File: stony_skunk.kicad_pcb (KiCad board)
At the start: 2 copper layers, 50 x 50 mm, 37 parts, among them P1 CURRENT/BUTTONS/DC, P2 LCD, P3 RELAY, P4 NFC, P5 FTDI, P6 RESET, P7 PROG, Q1 Q_NMOS_GSD, Q2 Q_NMOS_GSD, U1 NCP1117ST33T3G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

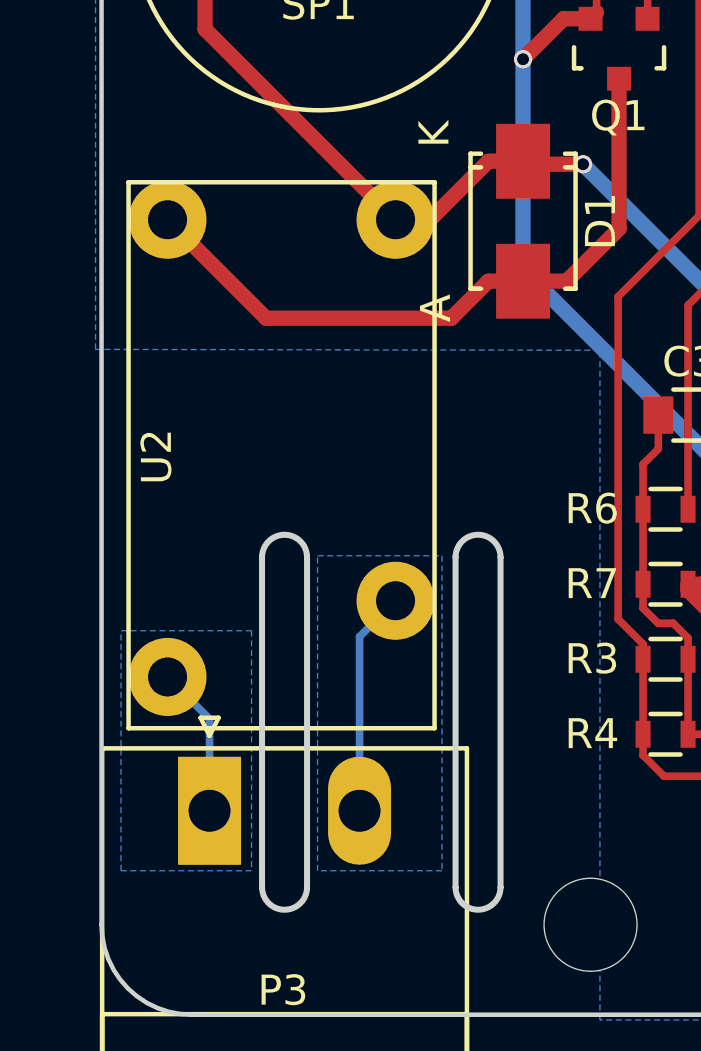
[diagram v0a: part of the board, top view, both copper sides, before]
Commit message: Flip relay to correct orientation
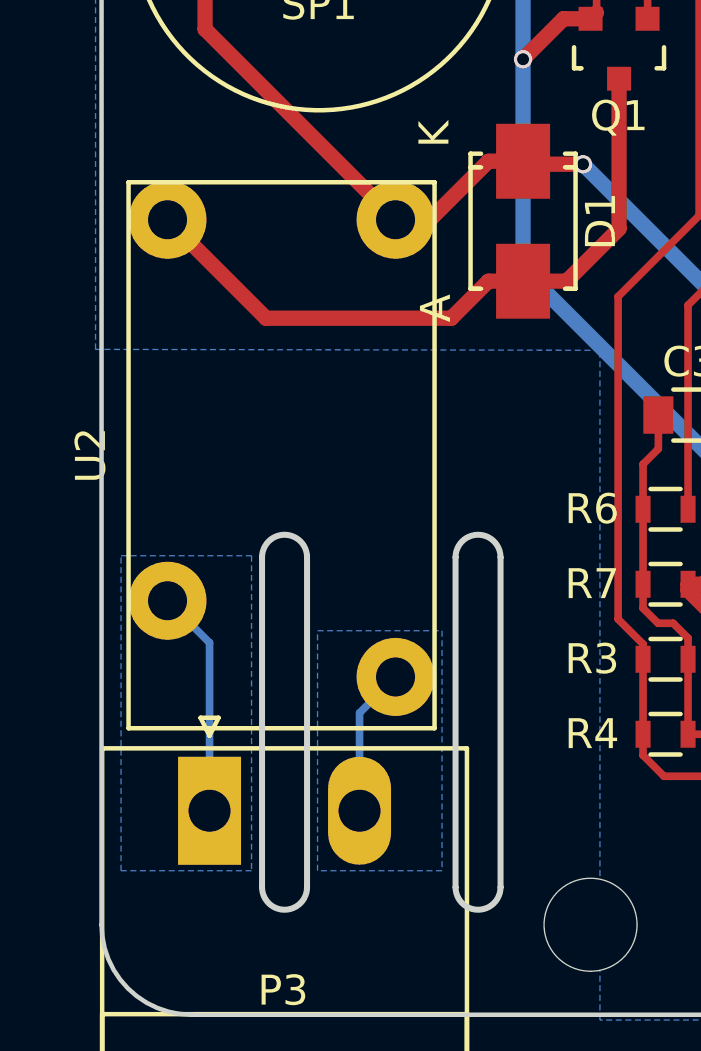
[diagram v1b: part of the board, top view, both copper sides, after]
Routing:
- net Net-(P3-Pad2): track 8.63 -> 4.96 mm
- net Net-(P3-Pad1): track 5.04 -> 7.58 mm
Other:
- board text added: "timhawes.com/ss2 edinburghhacklab.com"
- board text removed: "timhawes.com/ss1 edinburghhacklab.com"
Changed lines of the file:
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@@
-(kicad_pcb (version 4) (host pcbnew 4.0.4-stable)
+(kicad_pcb (version 4) (host pcbnew 4.0.4+dfsg1-stable)
   (general
     (links 76)
     (no_connects 0)
-    (area 60.374999 56.274999 110.525001 106.425001)
+    (area 56.149971 50.269799 114.800829 112.179)
     (thickness 1.6)
     (drawings 22)
-    (tracks 330)
+    (tracks 329)
     (zones 0)
     (modules 37)
@@
   (page A4)
   (layers
-    (0 F.Cu signal hide)
+    (0 F.Cu signal)
     (31 B.Cu signal)
     (32 B.Adhes user)
@@
     )
   )
-  (module timhawes:TE_OJ_RELAY (layer F.Cu)
-    (at 66.45 87.7 270)
-    (fp_text reference U2 (at 0.05 4.15 270) (layer F.SilkS)
-      (effects (font (size 1 1) (thickness 0.15)))
-    )
-    (fp_text value RELAY (at 0 7.75 270) (layer F.Fab)
-      (effects (font (size 1 1) (thickness 0.15)))
-    )
-    (fp_line (start -9.1 -5.1) (end 9.1 -5.1) (layer F.SilkS) (width 0.15))
-    (fp_line (start 9.1 -5.1) (end 9.1 5.1) (layer F.SilkS) (width 0.15))
-    (fp_line (start 9.1 5.1) (end -9.1 5.1) (layer F.SilkS) (width 0.15))
-    (fp_line (start -9.1 -5.1) (end -9.1 5.1) (layer F.SilkS) (width 0.15))
-    (pad 1 thru_hole circle (at -7.85 -3.8 270) (size 2.6 2.6) (drill 1.3) (layers *.Cu *.Mask)
-      (net 1 +5V))
-    (pad 2 thru_hole circle (at -7.85 3.8 270) (size 2.6 2.6) (drill 1.3) (layers *.Cu *.Mask)
-      (net 4 "Net-(D1-Pad2)"))
-    (pad 3 thru_hole circle (at 7.39 3.8 270) (size 2.6 2.6) (drill 1.3) (layers *.Cu *.Mask)
-      (net 8 "Net-(P3-Pad1)"))
-    (pad 4 thru_hole circle (at 4.85 -3.8 270) (size 2.6 2.6) (drill 1.3) (layers *.Cu *.Mask)
-      (net 9 "Net-(P3-Pad2)"))
-  )
   (module timhawes:MountingHole_M3+ (layer F.Cu)
     (at 107.45 95.4)
@@
     (pad "" np_thru_hole circle (at 0 0) (size 3.1 3.1) (drill 3.1) (layers *.Cu))
   )
+  (module timhawes:TE_OJ_RELAY (layer F.Cu)
+    (at 66.45 87.7 270)
+    (fp_text reference U2 (at 0 6.35 450) (layer F.SilkS)
+      (effects (font (size 1 1) (thickness 0.15)))
+    )
+    (fp_text value RELAY (at 0 7.75 270) (layer F.Fab)
+      (effects (font (size 1 1) (thickness 0.15)))
+    )
+    (fp_line (start -9.1 5.1) (end 9.1 5.1) (layer F.SilkS) (width 0.15))
+    (fp_line (start 9.1 5.1) (end 9.1 -5.1) (layer F.SilkS) (width 0.15))
+    (fp_line (start 9.1 -5.1) (end -9.1 -5.1) (layer F.SilkS) (width 0.15))
+    (fp_line (start -9.1 5.1) (end -9.1 -5.1) (layer F.SilkS) (width 0.15))
+    (pad 2 thru_hole circle (at -7.85 3.8 270) (size 2.6 2.6) (drill 1.3) (layers *.Cu *.Mask)
+      (net 4 "Net-(D1-Pad2)"))
+    (pad 1 thru_hole circle (at -7.85 -3.8 270) (size 2.6 2.6) (drill 1.3) (layers *.Cu *.Mask)
+      (net 1 +5V))
+    (pad 4 thru_hole circle (at 7.39 -3.8 270) (size 2.6 2.6) (drill 1.3) (layers *.Cu *.Mask)
+      (net 9 "Net-(P3-Pad2)"))
+    (pad 3 thru_hole circle (at 4.85 3.8 270) (size 2.6 2.6) (drill 1.3) (layers *.Cu *.Mask)
+      (net 8 "Net-(P3-Pad1)"))
+  )
   (gr_text - (at 104.4 98.8) (layer F.SilkS)
     (effects (font (size 1.5 1.5) (thickness 0.3)))
@@
     (effects (font (size 1.5 1.5) (thickness 0.3)))
   )
-  (gr_text "timhawes.com/ss1\nedinburghhacklab.com" (at 85.45 60.7) (layer B.SilkS)
+  (gr_text "timhawes.com/ss2\nedinburghhacklab.com" (at 85.45 60.7) (layer B.SilkS)
     (effects (font (size 1.5 1.5) (thickness 0.3)) (justify mirror))
   )
@@
   (segment (start 92.6846 96.1644) (end 96.3356 96.1644) (width 0.254) (layer F.Cu) (net 7))
   (segment (start 92.6846 93.6244) (end 92.6846 96.1644) (width 0.254) (layer F.Cu) (net 7))
-  (segment (start 64.05 99.55) (end 64.05 96.49) (width 0.254) (layer B.Cu) (net 8))
-  (segment (start 64.05 96.49) (end 62.65 95.09) (width 0.254) (layer B.Cu) (net 8))
-  (segment (start 69.05 99.55) (end 69.05 93.75) (width 0.254) (layer B.Cu) (net 9))
-  (segment (start 69.05 93.75) (end 70.25 92.55) (width 0.254) (layer B.Cu) (net 9))
-  (segment (start 68.75 98.7) (end 69.55 99.5) (width 0.25) (layer B.Cu) (net 9))
+  (segment (start 64.05 99.55) (end 64.05 93.95) (width 0.254) (layer B.Cu) (net 8))
+  (segment (start 64.05 93.95) (end 62.65 92.55) (width 0.254) (layer B.Cu) (net 8))
+  (segment (start 69.05 99.55) (end 69.05 96.29) (width 0.254) (layer B.Cu) (net 9))
+  (segment (start 69.05 96.29) (end 70.25 95.09) (width 0.254) (layer B.Cu) (net 9))
   (segment (start 103 68.3) (end 102.3 69) (width 0.254) (layer F.Cu) (net 10))
   (segment (start 102.3 69) (end 102.1 69) (width 0.254) (layer F.Cu) (net 10))
@@
     (polygon
       (pts
-        (xy 67.65 91.05) (xy 71.8 91.05) (xy 71.8 101.55) (xy 67.65 101.55)
+        (xy 67.65 93.55) (xy 71.8 93.55) (xy 71.8 101.55) (xy 67.65 101.55)
       )
     )
@@
     (min_thickness 0.254)
     (keepout (tracks not_allowed) (vias not_allowed) (copperpour not_allowed))
-    (fill yes (arc_segments 16) (thermal_gap 0.508) (thermal_bridge_width 0.508))
+    (fill (arc_segments 16) (thermal_gap 0.508) (thermal_bridge_width 0.508))
     (polygon
       (pts
@@
     (polygon
       (pts
-        (xy 65.45 93.55) (xy 65.45 101.55) (xy 61.1 101.55) (xy 61.1 93.55)
+        (xy 65.45 91.05) (xy 65.45 101.55) (xy 61.1 101.55) (xy 61.1 91.05)
       )
     )
@@
     (polygon
       (pts
-        (xy 67.65 91.05) (xy 71.8 91.05) (xy 71.8 101.55) (xy 67.65 101.55)
+        (xy 67.65 93.55) (xy 71.8 93.55) (xy 71.8 101.55) (xy 67.65 101.55)
       )
     )
@@
     (polygon
       (pts
-        (xy 61.1 93.55) (xy 65.45 93.55) (xy 65.45 101.55) (xy 61.1 101.55)
+        (xy 61.1 91.05) (xy 65.45 91.05) (xy 65.45 101.55) (xy 61.1 101.55)
       )
     )

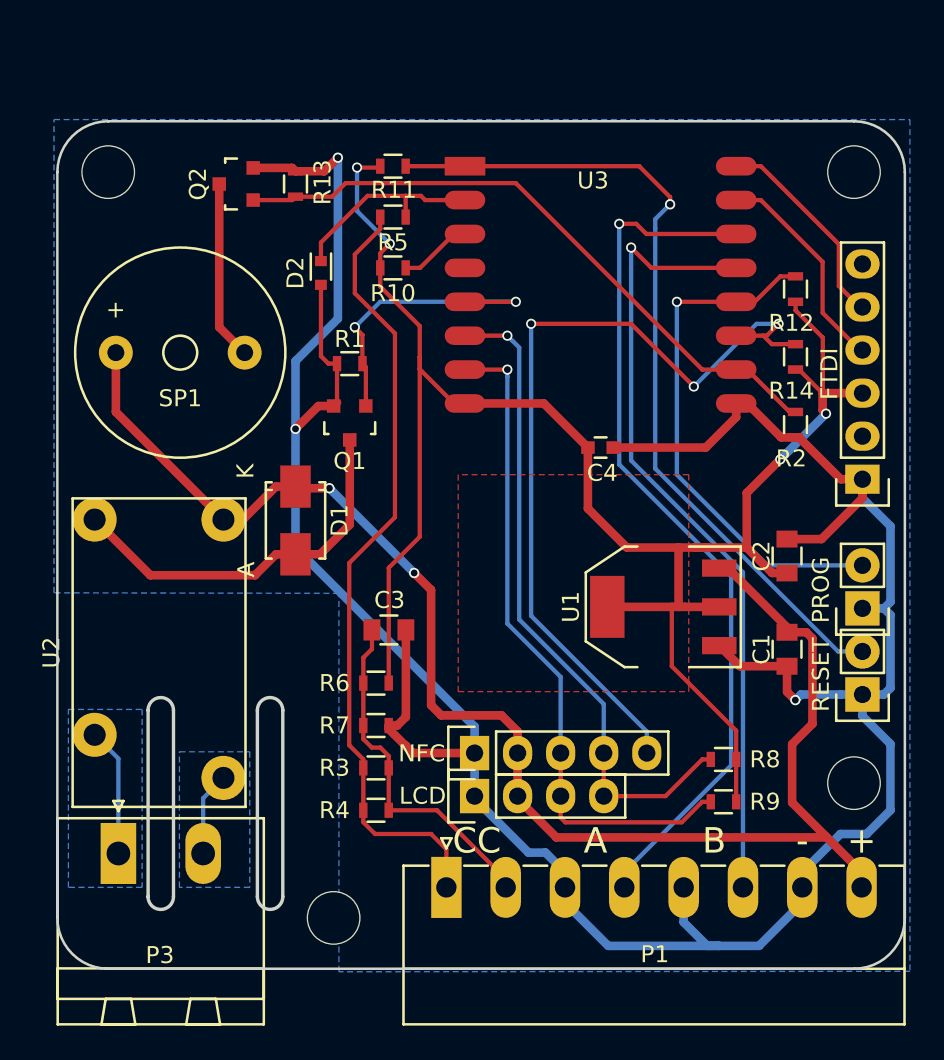
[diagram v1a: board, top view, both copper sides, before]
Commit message: Replace ESP12E with Wemos D1 Mini
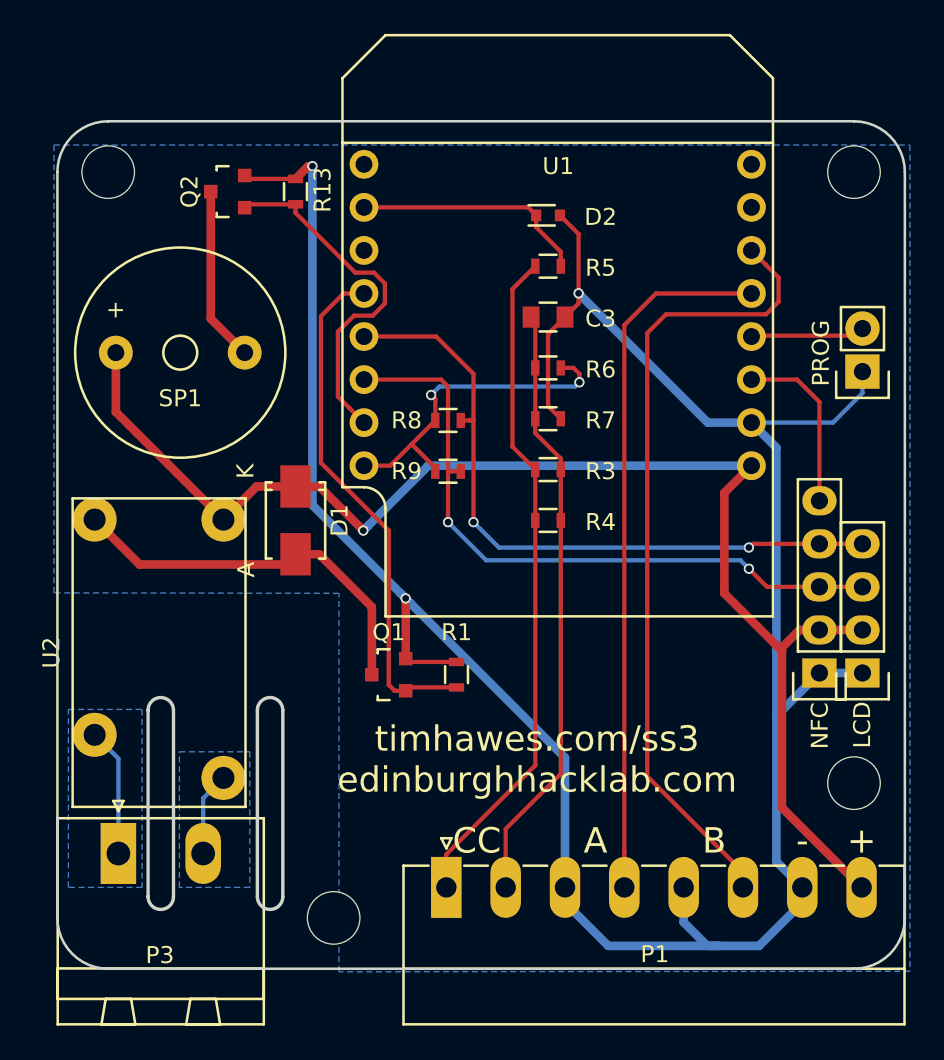
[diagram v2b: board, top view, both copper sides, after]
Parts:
- removed C1, C2: 10uF, Capacitors_SMD:C_0805
- removed C4: 0.1uF, Capacitors_SMD:C_0603
- removed P5: FTDI, Pin_Headers:Pin_Header_Straight_1x06
- removed P6: RESET, Pin_Headers:Pin_Header_Straight_1x02
- removed R10, R11, R12, R14, R2: 10K, Resistors_SMD:R_0603
- removed U3: ESP-12, timhawes:ESP-12
- P1: value CURRENT/BUTTONS/DC -> DC/BUTTONS/CURRENT
- U1: value NCP1117ST33T3G -> WEMOS_D1_MINI; footprint TO_SOT_Packages_SMD:SOT-223 -> timhawes:WEMOS_D1_MINI
- moved R8 25.8 mm to (83.5, 74.0), turned to 0 degrees
- moved R9 25.4 mm to (83.5, 77.0), turned to 0 degrees
- moved P2 24.0 mm to (108.0, 88.9), turned to 180 degrees
- moved R6 21.2 mm to (89.4, 70.9)
- moved P4 20.9 mm to (105.4, 88.9), turned to 180 degrees
- moved R7 20.8 mm to (89.4, 73.9)
- moved C3 20.7 mm to (89.4, 67.9)
- moved R3 20.3 mm to (89.4, 76.9)
- moved R4 19.9 mm to (89.4, 79.9)
- moved R1 19.4 mm to (84.0, 89.0), turned to 90 degrees
- moved U1 17.1 mm to (90.0, 69.0), turned to 0 degrees
- moved Q1 15.0 mm to (80.0, 89.0), turned to 90 degrees
- moved P7 14.0 mm to (108.0, 71.1)
- moved D2 13.8 mm to (89.4, 61.9), turned to 180 degrees
- moved R5 9.60 mm to (89.4, 64.9)
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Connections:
- U1 pad 1: GND -> Net-(U1-Pad1)
- U1 pad 2: +3V3 -> ADC
- U1 pad 3: +5V -> Net-(U1-Pad3)
- U1 pad 4: +3V3 -> RELAY
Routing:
- net +3V3: track 110.5 -> 19.9 mm, vias 4 -> 2
- net RESET: track 49.4 -> 0.00 mm, vias 1 -> 0
- net PN532_RESET: track 50.7 -> 10.4 mm, vias 3 -> 0
- net GPIO0: track 31.0 -> 6.74 mm, vias 1 -> 0
- net GND: track 170.4 -> 153.5 mm
- net BUZZER: track 38.0 -> 21.2 mm
- net CURRENT_B: track 21.0 -> 36.2 mm
- net RX: track 13.5 -> 0.00 mm
- net RELAY: track 18.0 -> 30.7 mm, vias 2 -> 0
- net TX: track 12.3 -> 0.00 mm
- net BUTTON_A: track 51.6 -> 41.4 mm, vias 1 -> 0
- net +5V: track 88.3 -> 81.4 mm, vias 2 -> 1
- net CURRENT_A: track 46.6 -> 39.9 mm
- net Net-(R10-Pad2): track 4.33 -> 0.00 mm
- net ADC: track 12.3 -> 14.0 mm
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- removed copper zone on F.Cu, net +3V3
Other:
- board text added: "timhawes.com/ss3 edinburghhacklab.com"
- board text removed: "timhawes.com/ss2 edinburghhacklab.com"

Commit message: Convert to Kicad v5 and fix mismatched reference in schematic (R2->R13)
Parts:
- R3, R4: value 22R -> 200R
- R6: value 56K -> 10K
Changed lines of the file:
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@@
-(kicad_pcb (version 4) (host pcbnew 4.0.7-e2-6376~60~ubuntu17.10.1)
+(kicad_pcb (version 20171130) (host pcbnew "(5.0.0-3-g5ebb6b6)")
   (general
-    (links 51)
-    (no_connects 0)
-    (area 60.374999 56.274999 110.525001 106.425001)
     (thickness 1.6)
     (drawings 22)
@@
     (visible_elements FFFEFF7F)
     (pcbplotparams
-      (layerselection 0x010f0_80000001)
+      (layerselection 0x010f0_ffffffff)
       (usegerberextensions true)
+      (usegerberattributes false)
+      (usegerberadvancedattributes false)
+      (creategerberjobfile false)
       (excludeedgelayer true)
       (linewidth 0.100000)
@@
       (hpglpennumber 1)
       (hpglpenspeed 20)
-      (hpglpendiameter 15)
-      (hpglpenoverlay 2)
+      (hpglpendiameter 15.000000)
       (psnegative false)
       (psa4output false)
@@
       (drillshape 0)
       (scaleselection 1)
-      (outputdirectory output/))
+      (outputdirectory "output/"))
   )
   (net 0 "")
@@
     (tags SOT-23)
     (attr smd)
-    (fp_text reference Q1 (at 2.5 0 360) (layer F.SilkS)
+    (fp_text reference Q1 (at 2.5 0) (layer F.SilkS)
       (effects (font (size 1 1) (thickness 0.15)))
     )
@@
       (net 7 SCL))
     (model Pin_Headers.3dshapes/Pin_Header_Straight_1x04.wrl
-      (at (xyz 0 -0.15 0))
+      (offset (xyz 0 -3.809999942779541 0))
       (scale (xyz 1 1 1))
       (rotate (xyz 0 0 90))
@@
       (net 10 PN532_RESET))
     (model Pin_Headers.3dshapes/Pin_Header_Straight_1x05.wrl
-      (at (xyz 0 -0.2 0))
+      (offset (xyz 0 -5.079999923706055 0))
       (scale (xyz 1 1 1))
       (rotate (xyz 0 0 90))
@@
       (net 11 GPIO0))
     (model Pin_Headers.3dshapes/Pin_Header_Straight_1x02.wrl
-      (at (xyz 0 -0.05 0))
+      (offset (xyz 0 -1.269999980926514 0))
       (scale (xyz 1 1 1))
       (rotate (xyz 0 0 90))
@@
     (tags "resistor 0603")
     (attr smd)
-    (fp_text reference R1 (at 2.5 0 360) (layer F.SilkS)
+    (fp_text reference R1 (at 2.5 0) (layer F.SilkS)
       (effects (font (size 1 1) (thickness 0.15)))
     )
@@
       (effects (font (size 1 1) (thickness 0.15)))
     )
-    (fp_text value 22R (at 0 1.9) (layer F.Fab)
+    (fp_text value 200R (at 0 1.9) (layer F.Fab)
       (effects (font (size 1 1) (thickness 0.15)))
     )
@@
       (effects (font (size 1 1) (thickness 0.15)))
     )
-    (fp_text value 22R (at 0 1.9) (layer F.Fab)
+    (fp_text value 200R (at 0 1.9) (layer F.Fab)
       (effects (font (size 1 1) (thickness 0.15)))
     )
@@
       (effects (font (size 1 1) (thickness 0.15)))
     )
-    (fp_text value 56K (at 0 1.9 180) (layer F.Fab)
+    (fp_text value 10K (at 0 1.9 180) (layer F.Fab)
       (effects (font (size 1 1) (thickness 0.15)))
     )
@@
   (module timhawes:TE_OJ_RELAY (layer F.Cu)
     (at 66.45 87.7 270)
-    (fp_text reference U2 (at 0 6.35 450) (layer F.SilkS)
-      (effects (font (size 1 1) (thickness 0.15)))
-    )
+    (fp_text reference U2 (at 0 6.35 90) (layer F.SilkS)
+      (effects (font (size 1 1) (thickness 0.15)))
+    )
